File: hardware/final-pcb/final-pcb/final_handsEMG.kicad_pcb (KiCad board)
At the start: 2 copper layers, 74 parts, among them J1 Conn_02x13_Odd_Even, U1 ADS1299CPAG, U2 STM32L496ZGT6

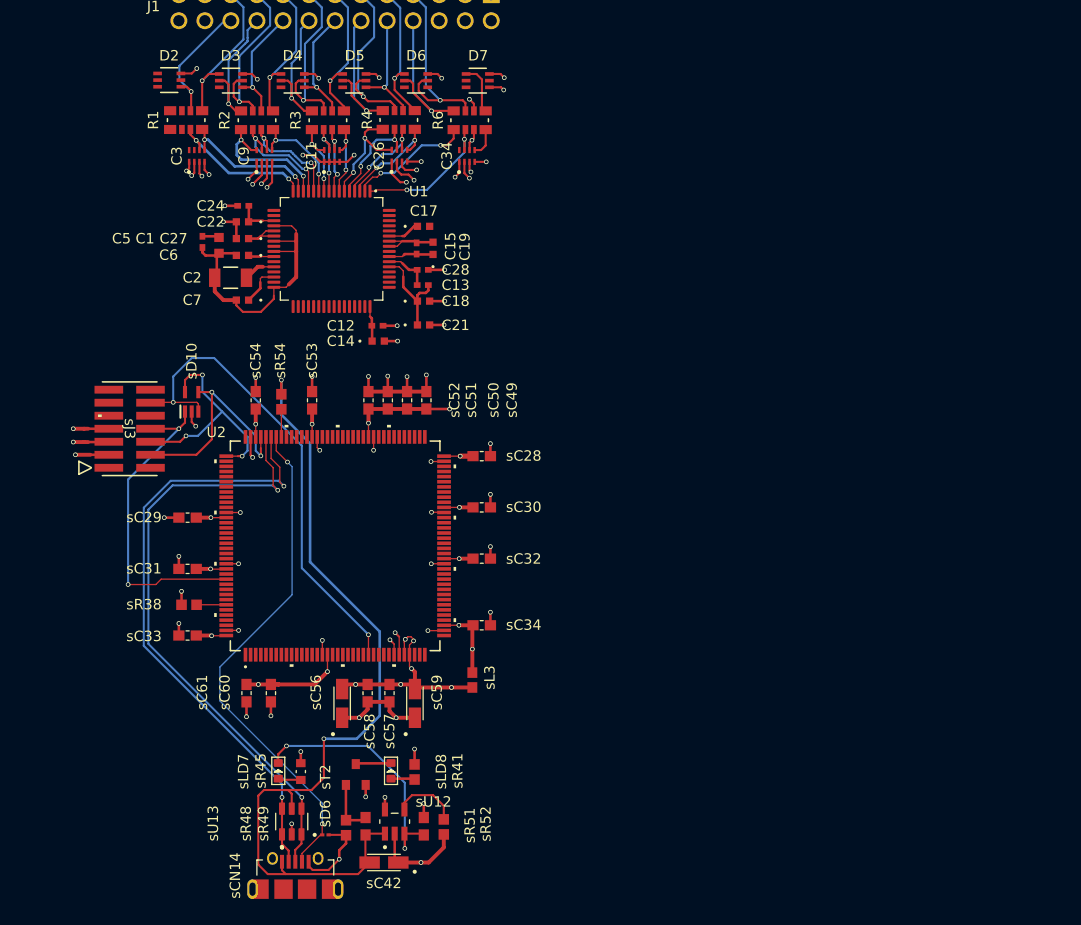
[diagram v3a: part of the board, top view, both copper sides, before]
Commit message: final pcb update 4.2.25 (added dongle usb stuff)
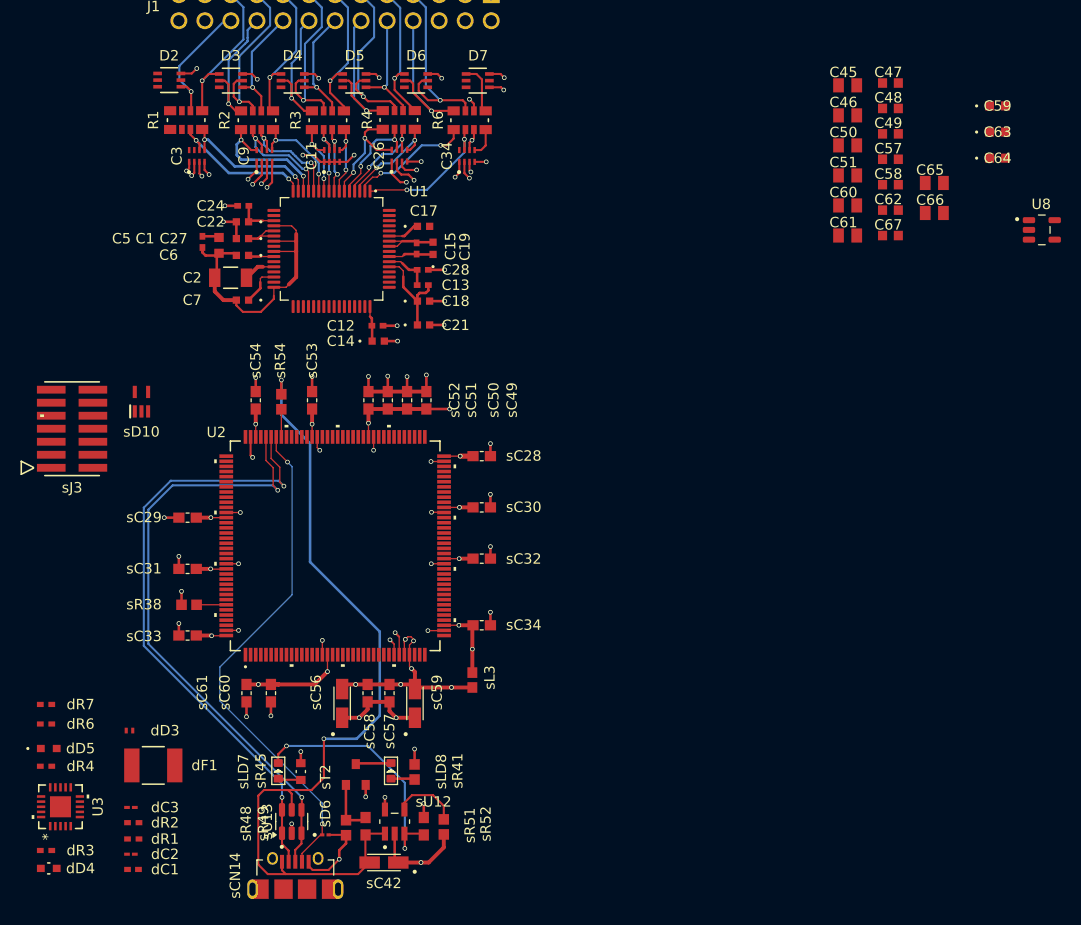
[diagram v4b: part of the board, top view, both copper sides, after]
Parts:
- added C45: 10uF, GRM219R61A106KE44D:CAPC2012X95N, F.Cu at (155.8, 45.0)
- added C46: 10uF, GRM219R61A106KE44D:CAPC2012X95N, F.Cu at (155.8, 48.0)
- added C47: 1uF, GRM188R61E105KA12D:CAPC1608X90N, F.Cu at (160.0, 44.8)
- added C48: 1uF, GRM188R61E105KA12D:CAPC1608X90N, F.Cu at (160.0, 47.3)
- added C49: 1uF, GRM188R61E105KA12D:CAPC1608X90N, F.Cu at (160.0, 49.8)
- added C50: 10uF, GRM219R61A106KE44D:CAPC2012X95N, F.Cu at (155.8, 50.9)
- added C51: 10uF, GRM219R61A106KE44D:CAPC2012X95N, F.Cu at (155.8, 53.8)
- added C57: 0.1uF, GRM188R71H104KA93D:CAPC1608X90N, F.Cu at (160.0, 52.3)
- added C58: 1uF, GRM188R61E105KA12D:CAPC1608X90N, F.Cu at (160.0, 54.7)
- added C59: 2.2uF, GRM185R60J225KE26D:CAP_GRM18_MUR, F.Cu at (170.5, 47.1)
- added C60: 10uF, GRM219R61A106KE44D:CAPC2012X95N, F.Cu at (155.8, 56.8)
- added C61: 10uF, GRM219R61A106KE44D:CAPC2012X95N, F.Cu at (155.8, 59.7)
- added C62: 1uF, GRM188R61E105KA12D:CAPC1608X90N, F.Cu at (160.0, 57.2)
- added C63: 2.2uF, GRM185R60J225KE26D:CAP_GRM18_MUR, F.Cu at (170.5, 49.6)
- added C64: 2.2uF, GRM185R60J225KE26D:CAP_GRM18_MUR, F.Cu at (170.5, 52.1)
- added C65: 10uF, GRM219R61A106KE44D:CAPC2012X95N, F.Cu at (164.3, 54.6)
- added C66: 10uF, GRM219R61A106KE44D:CAPC2012X95N, F.Cu at (164.3, 57.5)
- added C67: 0.01uF, GRM188R71H103KA01D:CAPC1608X90N, F.Cu at (160.0, 59.7)
- added U3: FT231XQ-R, FT231XQ-R:QFN20_FT231XQ_FTD, F.Cu at (79.1, 115.4)
- added U8: TPS72325DBVT, TPS72325DBVT:SOT95P280X145-5N, F.Cu at (174.8, 59.1)
- added dC1: 0.01uF, CC0402KRX7R7BB103:CC0402N_YAG, F.Cu at (86.1, 121.5)
- added dC2: 47pF, GRM0335C1E470JA01D:G-033_MUR, F.Cu at (85.9, 120.1)
- added dC3: 47pF, GRM0335C1E470JA01D:G-033_MUR, F.Cu at (85.9, 115.5)
- added dD3: D_Small, ESDALC6V1-1M2:SOD882_STM, F.Cu at (85.8, 108.0)
- added dD4: RED, LTST-C191KRKT:LED_LTST-C191KRKT_LTO, F.Cu at (77.9, 121.4)
- added dD5: GREEN, LTST-C191KGKT:LED_LTST-C191KGKT_LTO, F.Cu at (77.9, 109.8)
- added dF1: Fuse_Small, MF-MSMF050-2:FUSE_F050-2, F.Cu at (88.1, 111.4)
- added dR1: 27, RC0402FR-0722RL:RC0402N_YAG, F.Cu at (86.2, 118.6)
- added dR2: 27, RC0402FR-0722RL:RC0402N_YAG, F.Cu at (86.2, 117.0)
- added dR3: 330, RC0402JR-07330RL:RC0402N_YAG, F.Cu at (77.6, 119.7)
- added dR4: 330, RC0402JR-07330RL:RC0402N_YAG, F.Cu at (77.6, 111.5)
- added dR6: 1K, RT0402FRE071KL:RC0402N_YAG, F.Cu at (77.6, 107.4)
- added dR7: 1K, RT0402FRE071KL:RC0402N_YAG, F.Cu at (77.6, 105.5)
- sU13: footprint USBLC6-2SC6:SOT95P280X145-6N -> Package_TO_SOT_SMD:SOT-23-6
- moved sJ3 5.62 mm to (80.2, 78.5)
- moved sD10 4.90 mm to (87.0, 75.9)
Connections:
- C12 pad 1: DVDD -> AVOUT3
- C14 pad 1: DVDD -> AVOUT3
- C34 pad 8: IN8N -> IN8P
- U1 pad 48: DVDD -> AVOUT3
- U1 pad 50: DVDD -> AVOUT3
- sC28 pad 1: DVDD -> AVOUT3
- sC29 pad 1: DVDD -> AVOUT3
- sC30 pad 1: DVDD -> AVOUT3
- sC31 pad 1: DVDD -> AVOUT3
- sC32 pad 1: DVDD -> AVOUT3
- sC33 pad 1: DVDD -> AVOUT3
- sC34 pad 1: DVDD -> AVOUT3
- sC49 pad 1: DVDD -> AVOUT3
- sC50 pad 1: DVDD -> AVOUT3
- sC51 pad 1: DVDD -> AVOUT3
- sC52 pad 1: DVDD -> AVOUT3
- sC53 pad 1: DVDD -> AVOUT3
- sC54 pad 1: DVDD -> AVOUT3
- sC56 pad : AVDD -> (no net)
- sC56 pad -: GNDA -> (no net)
- sC59 pad +: AVDD -> (no net)
- sC59 pad -: GNDA -> (no net)
- sC60 pad 1: DVDD -> AVOUT3
- sC61 pad 1: DVDD -> AVOUT3
- sCN14 pad 1: USB_VBUS -> Net-(sCN14-VBUS)
- sCN14 pad 2: USB_DN -> Net-(sCN14-D-)
- sCN14 pad 3: USB_DP -> Net-(sCN14-D+)
- sJ3 pad 3: DVDD -> AVOUT3
- sL3 pad 1: DVDD -> AVOUT3
- sLD7 pad +: Net-(sLD7-A) -> (no net)
- sLD7 pad -: Net-(sLD7-K) -> (no net)
- sLD8 pad +: Net-(sLD8-A) -> (no net)
- sLD8 pad -: Net-(sLD8-K) -> (no net)
- sR41 pad 2: DVDD -> AVOUT3
- sR45 pad 2: DVDD -> AVOUT3
- sR49 pad 2: USB_VBUS -> AVBUS
- sR51 pad 2: DVDD -> AVOUT3
- sU12 pad 1: USB_VBUS -> AVBUS
- sU12 pad 5: DVDD -> AVOUT3
- sU13 pad 5: USB_VBUS -> AVBUS
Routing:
- net NRST: track 48.1 -> 0.00 mm, vias 2 -> 0
- net PB3: track 31.7 -> 0.00 mm, vias 2 -> 0
- net PA14: track 23.3 -> 0.00 mm, vias 3 -> 0
- net PA13: track 22.6 -> 0.00 mm, vias 2 -> 0
- net DVDD: track 63.9 -> 51.9 mm, vias 19 -> 14
- net AVOUT3: track 0.00 -> 8.67 mm, vias 0 -> 4
- net GND: track 71.3 -> 62.7 mm, vias 34 -> 31

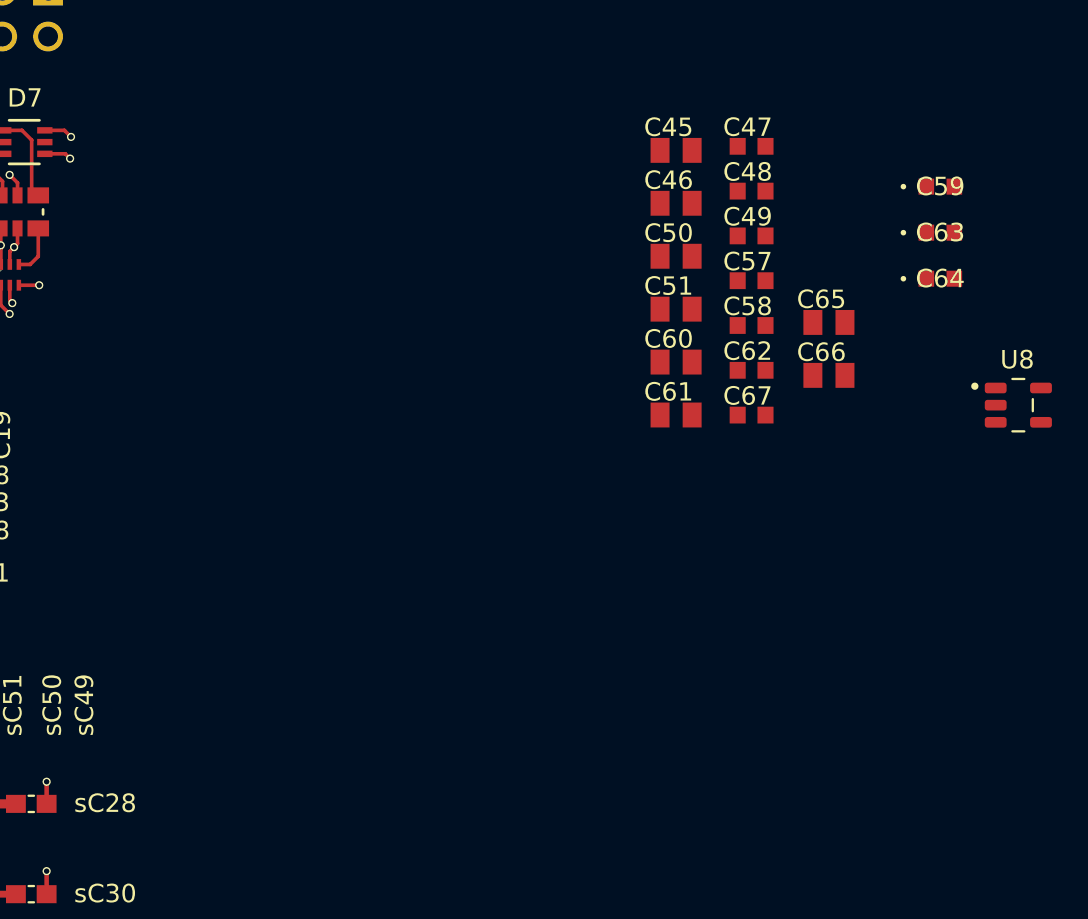
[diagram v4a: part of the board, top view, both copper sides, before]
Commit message: Added ECG portions to the final, corrected -5 points
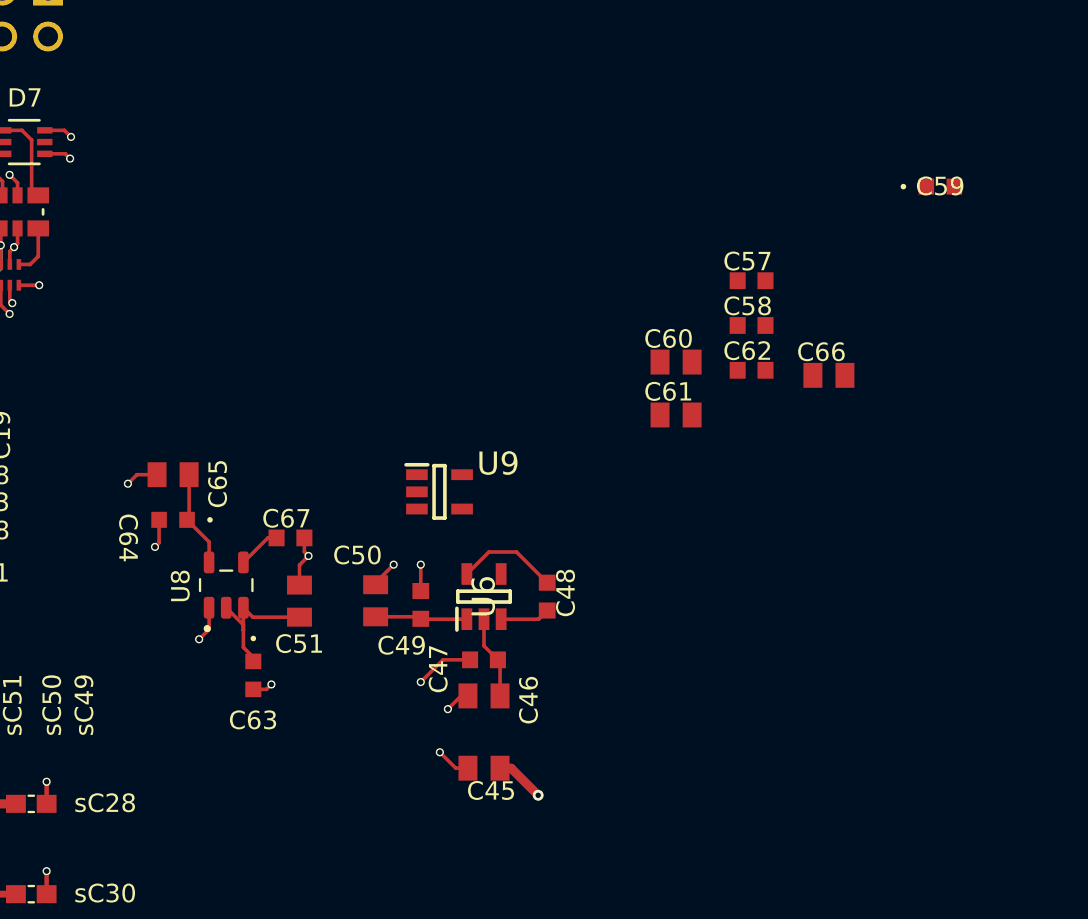
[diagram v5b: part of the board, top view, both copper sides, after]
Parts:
- added U6: TPS60403DBVT, TPS60403DBVT:SOT95P280X145-5N, F.Cu at (145.2, 69.8)
- added U9: TPS73225DBVT, TPS60403DBVT:SOT95P280X145-5N, F.Cu at (142.8, 64.0)
- moved C63 45.2 mm to (132.4, 74.1), turned to -90 degrees
- moved U8 45.0 mm to (130.9, 69.1), turned to 90 degrees
- moved C64 44.5 mm to (128.0, 65.5), turned to 180 degrees
- moved C65 37.3 mm to (128.0, 63.0), turned to 180 degrees
- moved C45 35.8 mm to (145.2, 79.2), turned to 180 degrees
- moved C47 32.1 mm to (145.2, 73.2), turned to 180 degrees
- moved C46 29.3 mm to (145.2, 75.2), turned to 180 degrees
- moved C49 27.4 mm to (141.7, 70.2), turned to 90 degrees
- moved C67 26.4 mm to (134.5, 66.5)
- moved C51 26.4 mm to (135.0, 70.0), turned to 90 degrees
- moved C50 25.3 mm to (139.2, 70.0), turned to 90 degrees
- moved C48 25.1 mm to (148.7, 69.8), turned to -90 degrees
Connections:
- C51 pad 1: -5V -> -5VCC
- C63 pad 1: 5VCC -> -5VCC
- U8 pad 2: 5VCC -> -5VCC
- U8 pad 3: 5VCC -> -5VCC
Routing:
- net GNDA: track 74.9 -> 94.1 mm, vias 38 -> 48
- net -5VCC: track 0.00 -> 13.5 mm
- net Net-(U6-CFLY+): track 0.00 -> 5.66 mm
- net Net-(U8-OUT): track 0.00 -> 5.41 mm
- net 5VCC: track 0.00 -> 4.62 mm
- net Net-(U6-CFLY-): track 0.00 -> 2.75 mm
- net AVOUT4: track 0.00 -> 2.73 mm, vias 0 -> 1
- net Net-(U8-NR): track 0.00 -> 2.40 mm
